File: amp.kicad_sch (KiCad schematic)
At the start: 22 parts, among them J4 PinHeader_1x2_P2.54mm_Drill1.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, J5 Phone_TRS_MiniJack_SJ-3523-SM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, U3 TAS2505IRGER, Y2 Oscillator_50MHz_ECS_1612MV

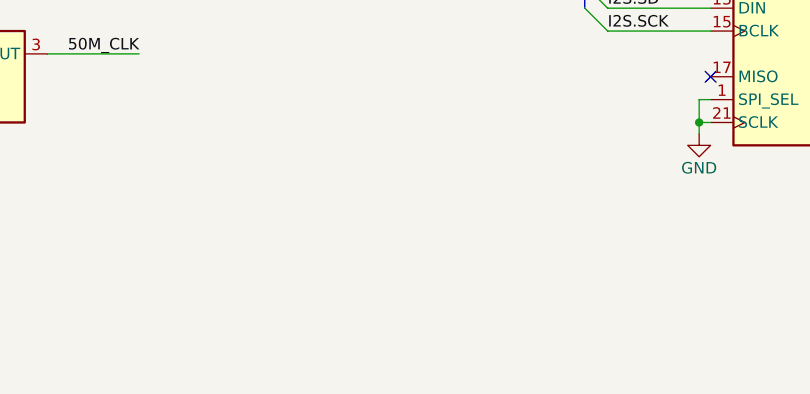
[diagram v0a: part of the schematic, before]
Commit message: [#71555] Add new root sheet structure
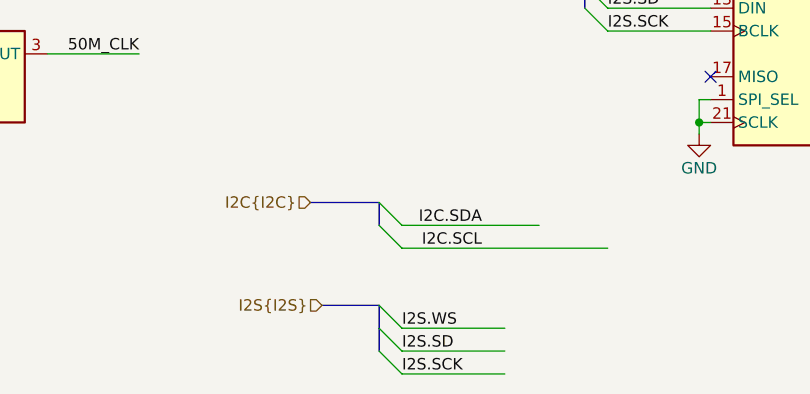
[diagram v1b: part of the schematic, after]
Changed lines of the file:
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@@
+	)
+	(bus_entry
+		(at 133.35 156.21)
+		(size 2.54 2.54)
+		(stroke
+			(width 0)
+			(type default)
+		)
 	)
 	(bus_entry
@@
 	)
 	(bus_entry
+		(at 133.35 144.78)
+		(size 2.54 2.54)
+		(stroke
+			(width 0)
+			(type default)
+		)
+	)
+	(bus_entry
 		(at 156.21 120.65)
 		(size 2.54 2.54)
@@
 		)
 	)
+	(bus_entry
+		(at 133.35 142.24)
+		(size 2.54 2.54)
+		(stroke
+			(width 0)
+			(type default)
+		)
+	)
+	(bus_entry
+		(at 133.35 158.75)
+		(size 2.54 2.54)
+		(stroke
+			(width 0)
+			(type default)
+		)
+	)
+	(bus_entry
+		(at 133.35 153.67)
+		(size 2.54 2.54)
+		(stroke
+			(width 0)
+			(type default)
+		)
+	)
 	(wire
 		(pts
@@
 		)
 	)
+	(bus
+		(pts
+			(xy 133.35 156.21) (xy 133.35 158.75)
+		)
+		(stroke
+			(width 0)
+			(type default)
+		)
+	)
 	(wire
 		(pts
@@
 	(wire
 		(pts
+			(xy 135.89 144.78) (xy 151.13 144.78)
+		)
+		(stroke
+			(width 0)
+			(type default)
+		)
+	)
+	(wire
+		(pts
 			(xy 59.69 81.28) (xy 59.69 82.55)
 		)
@@
 	(wire
 		(pts
+			(xy 135.89 147.32) (xy 158.75 147.32)
+		)
+		(stroke
+			(width 0)
+			(type default)
+		)
+	)
+	(wire
+		(pts
 			(xy 76.2 125.73) (xy 77.47 125.73)
 		)
@@
 	(wire
 		(pts
+			(xy 135.89 158.75) (xy 147.32 158.75)
+		)
+		(stroke
+			(width 0)
+			(type default)
+		)
+	)
+	(wire
+		(pts
 			(xy 199.39 130.81) (xy 199.39 133.35)
 		)
@@
 	(wire
 		(pts
+			(xy 135.89 156.21) (xy 147.32 156.21)
+		)
+		(stroke
+			(width 0)
+			(type default)
+		)
+	)
+	(wire
+		(pts
 			(xy 210.82 110.49) (xy 210.82 115.57)
 		)
@@
 		)
 	)
+	(wire
+		(pts
+			(xy 135.89 161.29) (xy 147.32 161.29)
+		)
+		(stroke
+			(width 0)
+			(type default)
+		)
+	)
 	(bus
 		(pts
@@
 		)
 	)
+	(bus
+		(pts
+			(xy 125.73 142.24) (xy 133.35 142.24)
+		)
+		(stroke
+			(width 0)
+			(type default)
+		)
+	)
 	(wire
 		(pts
@@
 		)
 	)
+	(bus
+		(pts
+			(xy 133.35 142.24) (xy 133.35 144.78)
+		)
+		(stroke
+			(width 0)
+			(type default)
+		)
+	)
 	(wire
 		(pts
@@
 		)
 	)
+	(bus
+		(pts
+			(xy 127 153.67) (xy 133.35 153.67)
+		)
+		(stroke
+			(width 0)
+			(type default)
+		)
+	)
 	(wire
 		(pts
@@
 		(pts
 			(xy 102.87 88.9) (xy 102.87 85.09)
+		)
+		(stroke
+			(width 0)
+			(type default)
+		)
+	)
+	(bus
+		(pts
+			(xy 133.35 153.67) (xy 133.35 156.21)
 		)
 		(stroke
@@
 		)
 	)
+	(label "I2C.SDA"
+		(at 144.78 144.78 180)
+		(fields_autoplaced yes)
+		(effects
+			(font
+				(size 1.27 1.27)
+			)
+			(justify right bottom)
+		)
+	)
+	(label "I2S.WS"
+		(at 135.89 156.21 0)
+		(fields_autoplaced yes)
+		(effects
+			(font
+				(size 1.27 1.27)
+			)
+			(justify left bottom)
+		)
+	)
 	(label "AVDD"
 		(at 208.28 77.47 0)
@@
 		)
 	)
+	(label "I2C.SCL"
+		(at 144.78 147.32 180)
+		(fields_autoplaced yes)
+		(effects
+			(font
+				(size 1.27 1.27)
+			)
+			(justify right bottom)
+		)
+	)
 	(label "IOVDD"
 		(at 111.76 64.77 180)
@@
 		)
 	)
+	(label "I2S.SD"
+		(at 135.89 158.75 0)
+		(fields_autoplaced yes)
+		(effects
+			(font
+				(size 1.27 1.27)
+			)
+			(justify left bottom)
+		)
+	)
 	(label "IOVDD"
 		(at 58.42 81.28 180)
@@
 			)
 			(justify right bottom)
+		)
+	)
+	(label "I2S.SCK"
+		(at 135.89 161.29 0)
+		(fields_autoplaced yes)
+		(effects
+			(font
+				(size 1.27 1.27)
+			)
+			(justify left bottom)
 		)
 	)
@@
 		(fields_autoplaced yes)
 		(effects
+			(font
+				(size 1.27 1.27)
+			)
+			(justify right)
+		)
+	)
+	(hierarchical_label "I2C{I2C}"
+		(shape input)
+		(at 125.73 142.24 180)
+		(fields_autoplaced yes)
+		(effects
+			(font
+				(size 1.27 1.27)
+			)
+			(justify right)
+		)
+	)
+	(hierarchical_label "I2S{I2S}"
+		(shape input)
+		(at 127 153.67 180)
+		(fields_autoplaced yes)
+		(effects

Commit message: [#71555] Prepare sch for AMP
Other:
- moved on the sheet: C18, C19, C20, C21, C22, C23, C24, C25, C26, C27, J4, J5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

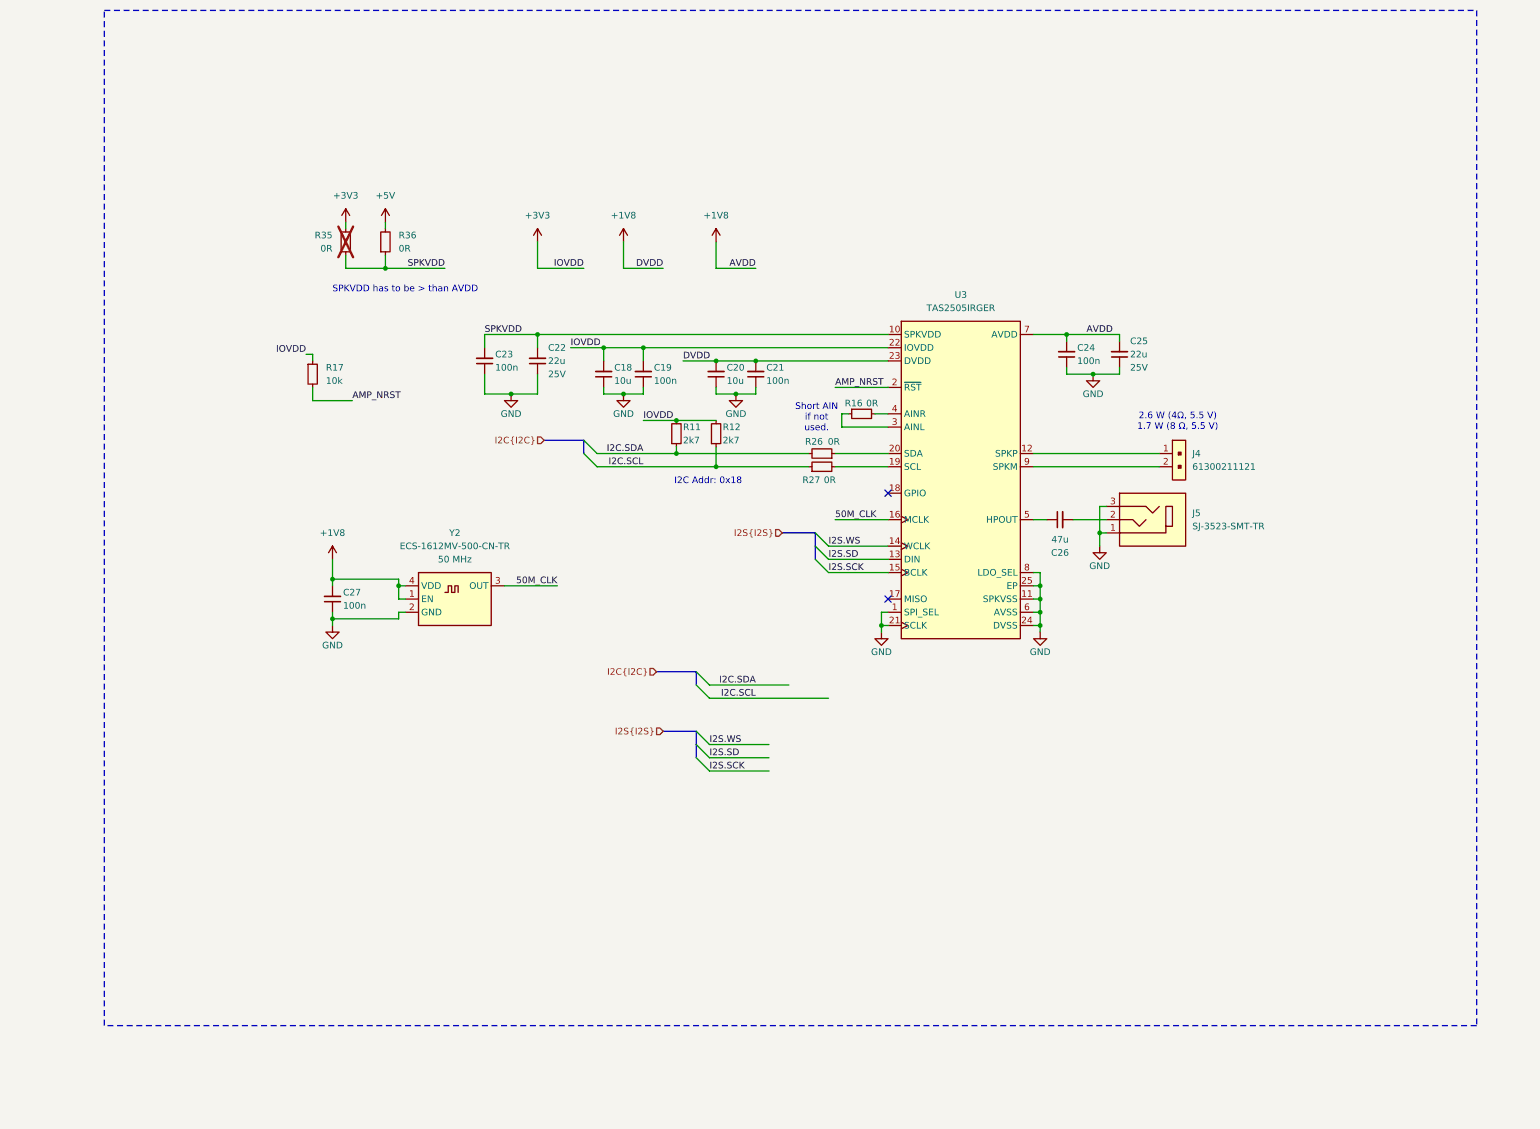
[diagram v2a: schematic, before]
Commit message: [#71555] Add connections between RP2040s
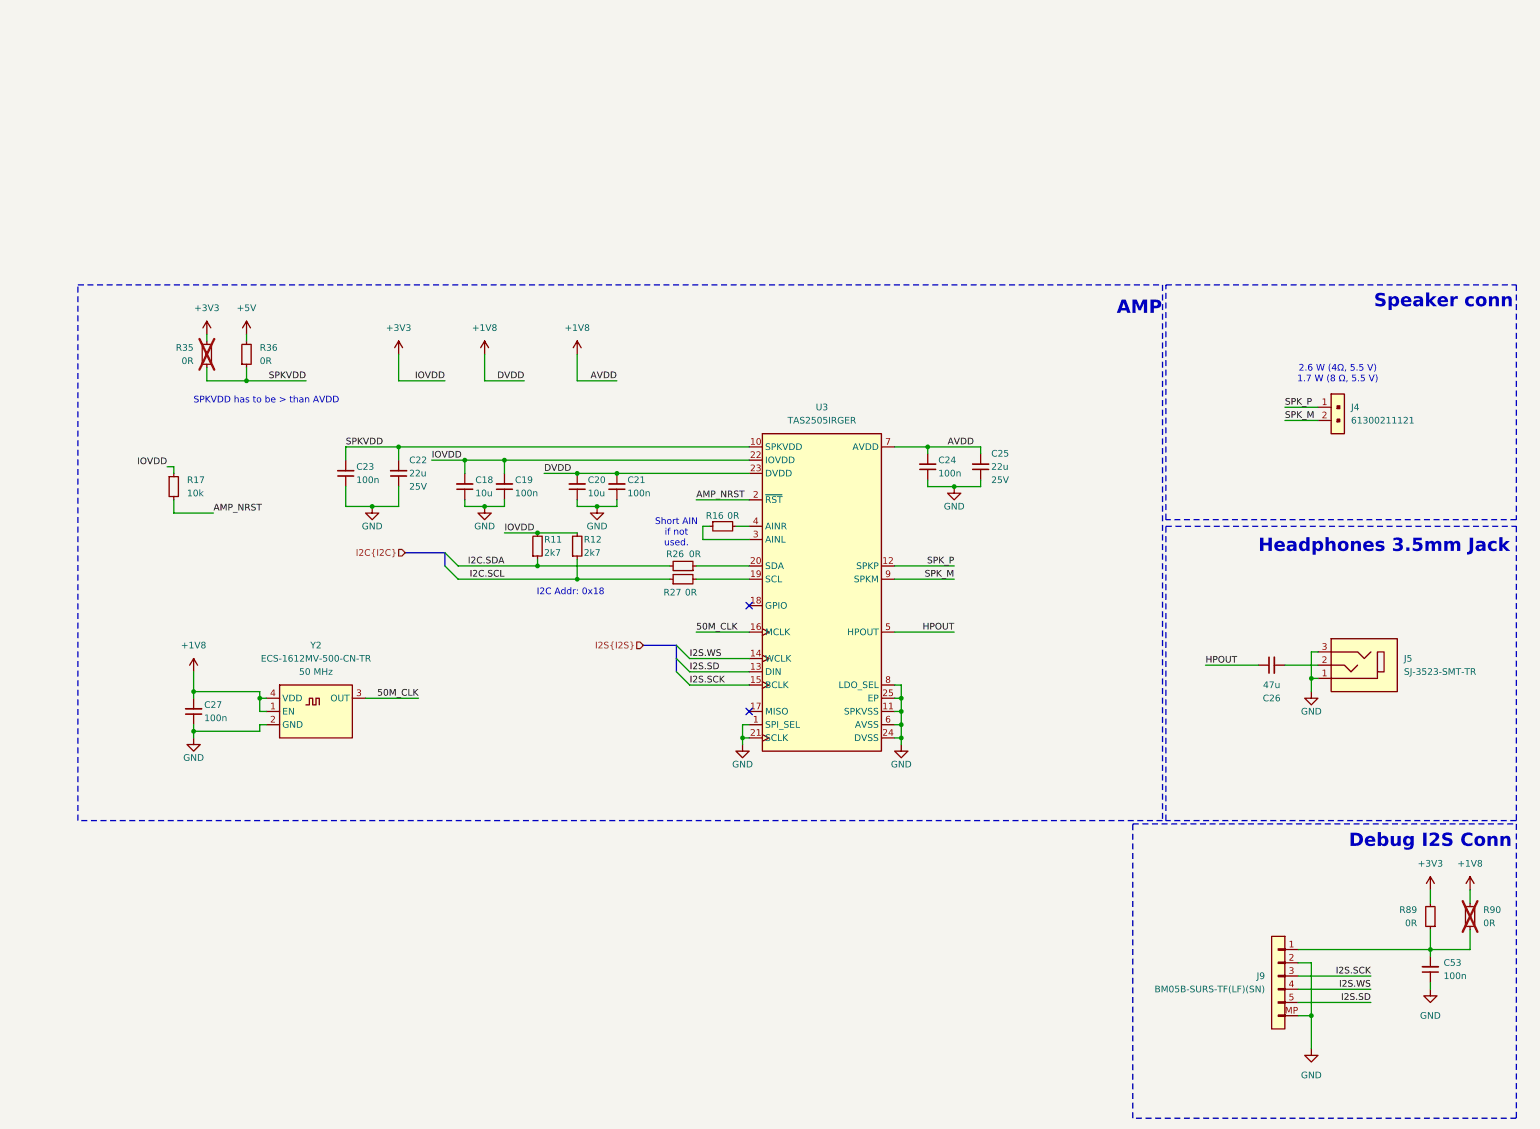
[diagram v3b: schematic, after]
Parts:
- added C53: C_100n_0402, antmicro-footprints:C_0402_1005Metric, symbol antmicroCapacitors0402:C_100n_0402
- added J9: JST_SUR_1x5_BM05B-SURS-TB-LF-SN, antmicro-footprints:Conn_JST_SUR_1x5_BM05B-SURS-TF-LF-SN, symbol antmicroWire2BoardConnectors:JST_SUR_1x5_BM05B-SURS-TB-LF-SN
- added R89, R90: R_0R_0402, antmicro-footprints:R_0402_1005Metric, symbol antmicroResistors0402:R_0R_0402
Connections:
- net +1V8: now also R90.2
- net +3V3: now also R89.2
- net GND: now also C53.1, J9.2, J9.MP
- net I2S.SCK: now also J9.3
- net I2S.SD: now also J9.5
- net I2S.WS: now also J9.4
- net SPK_P: now reaches J4.1, U3.12 (SPKP)
- net HPOUT: now reaches C26.1, U3.5 (HPOUT)
- net SPK_M: now reaches J4.2, U3.9 (SPKM)
- new net: C53.2, J9.1, R89.1, R90.1
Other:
- note added: "AMP"
- note added: "Debug I2S Conn"
- note added: "Headphones 3.5mm Jack"
- note added: "Speaker conn"
- moved on the sheet: C18, C19, C20, C21, C22, C23, C24, C25, C26, C27, J4, J5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

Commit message: [#71555] Resolve ERC
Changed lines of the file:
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@@
+	)
+	(symbol
+		(lib_id "antmicropower:PWR_FLAG")
+		(at 107.95 110.49 270)
+		(unit 1)
+		(exclude_from_sim no)
+		(in_bom yes)
+		(on_board yes)
+		(dnp no)
+		(fields_autoplaced yes)
+		(property "Reference" "#FLG07"
+			(at 109.855 110.49 0)
+			(effects
+				(font
+					(size 1.27 1.27)
+				)
+				(hide yes)
+			)
+		)
+		(property "Value" "PWR_FLAG"
+			(at 111.76 110.4899 90)
+			(effects
+				(font
+					(size 1.27 1.27)
+				)
+				(justify left)
+			)
+		)
+		(property "Footprint" ""
+			(at 107.95 110.49 0)
+			(effects
+				(font
+					(size 1.27 1.27)
+				)
+				(hide yes)
+			)
+		)
+		(property "Datasheet" ""
+			(at 107.95 110.49 0)
+			(effects
+				(font
+					(size 1.27 1.27)
+				)
+				(hide yes)
+			)
+		)
+		(property "Description" ""
+			(at 107.95 110.49 0)
+			(effects
+				(font
+					(size 1.27 1.27)
+				)
+				(hide yes)
+			)
+		)
+		(pin "1"
+		)
+		(instances
+			(project ""
+				(path "/7fb12ebf-f685-4412-b638-445b1bf344bc/80300fa7-dce3-4149-8e27-6609cbfb608d"
+					(reference "#FLG07")
+					(unit 1)
+				)
+			)
+		)
 	)
 	(symbol

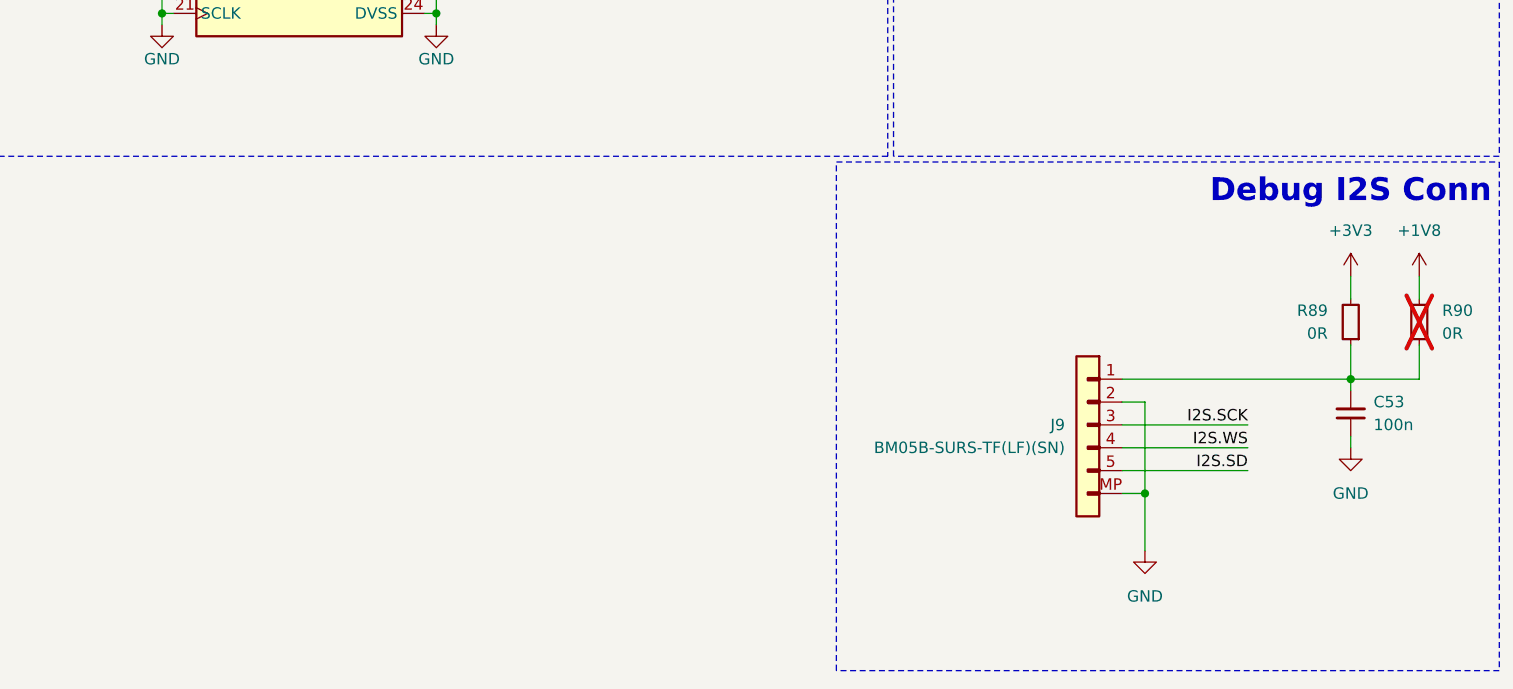
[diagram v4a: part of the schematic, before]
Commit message: [#71555] Add debug I2S conn
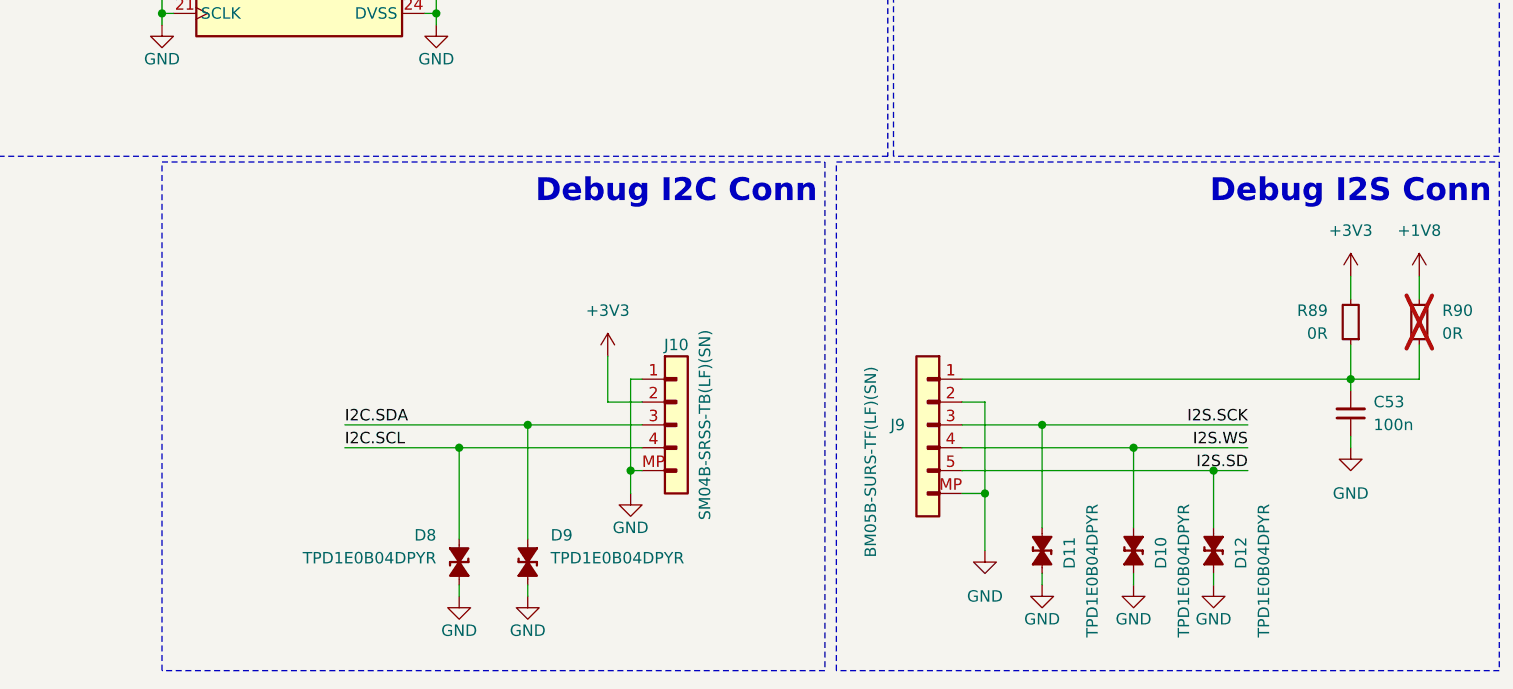
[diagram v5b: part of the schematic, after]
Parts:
- added D10, D11, D12, D8, D9: TPD1E0B04_XDFN-2, antmicro-footprints:XDFN-2_1x0.60mm, symbol antmicroTVSDiodes:TPD1E0B04_XDFN-2
- added J10: JST_SH_1x4_SM04B-SRSS-TB-LF-SN, antmicro-footprints:Conn_JST_SH_1x4_SM04B-SRSS-TB-LF-SN, symbol antmicroWire2BoardConnectors:JST_SH_1x4_SM04B-SRSS-TB-LF-SN
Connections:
- net +3V3: now also J10.2
- net GND: now also D10.1 (C), D11.1 (C), D12.1 (C), D8.1 (C), D9.1 (C), J10.1, J10.MP
- net I2C.SCL: now also D8.2 (A), J10.4
- net I2C.SDA: now also D9.2 (A), J10.3
- net I2S.SCK: now also D11.2 (A)
- net I2S.SD: now also D12.2 (A)
- net I2S.WS: now also D10.2 (A)
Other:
- note added: "Debug I2C Conn"
- moved on the sheet: J9
